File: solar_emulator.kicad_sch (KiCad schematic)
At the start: 57 parts, among them J1 USB_C_Receptacle, J2 Conn_01x02, J3 Conn_01x03, J4 Conn_01x02, J5 Conn_01x02, J6 Conn_01x04, J7 Conn_01x02, Q1 NMOS, Q2 NMOS, Q3 NMOS, Q4 NMOS, Q5 NMOS, Q6 NMOS, Q7 NMOS, Q8 NMOS, SW1 SW_Push, SW2 SW_Push, U1 ESP32-S3-WROOM-1, U2 LD1117S33TR_SOT223, U3 HIP4081AIPZ, U4 HIP4081AIPZ

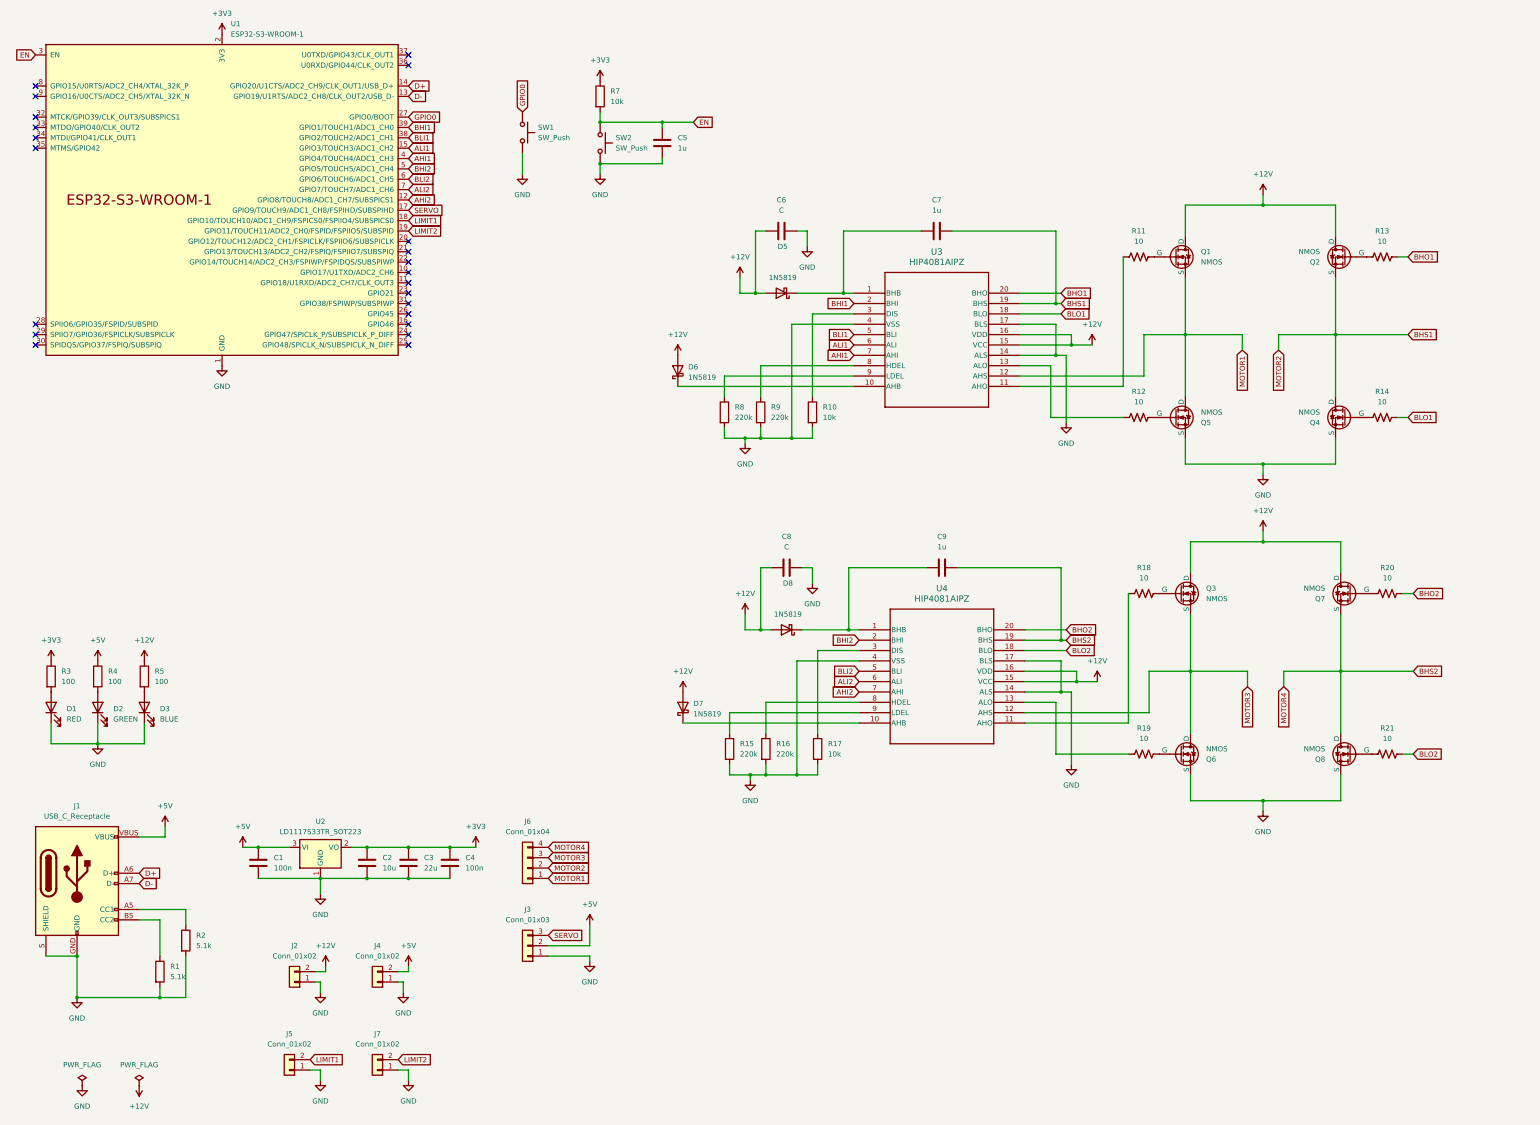
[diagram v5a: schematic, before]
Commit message: assign footprints, import footprints to pcb
start placing components on pcb, seek for advice
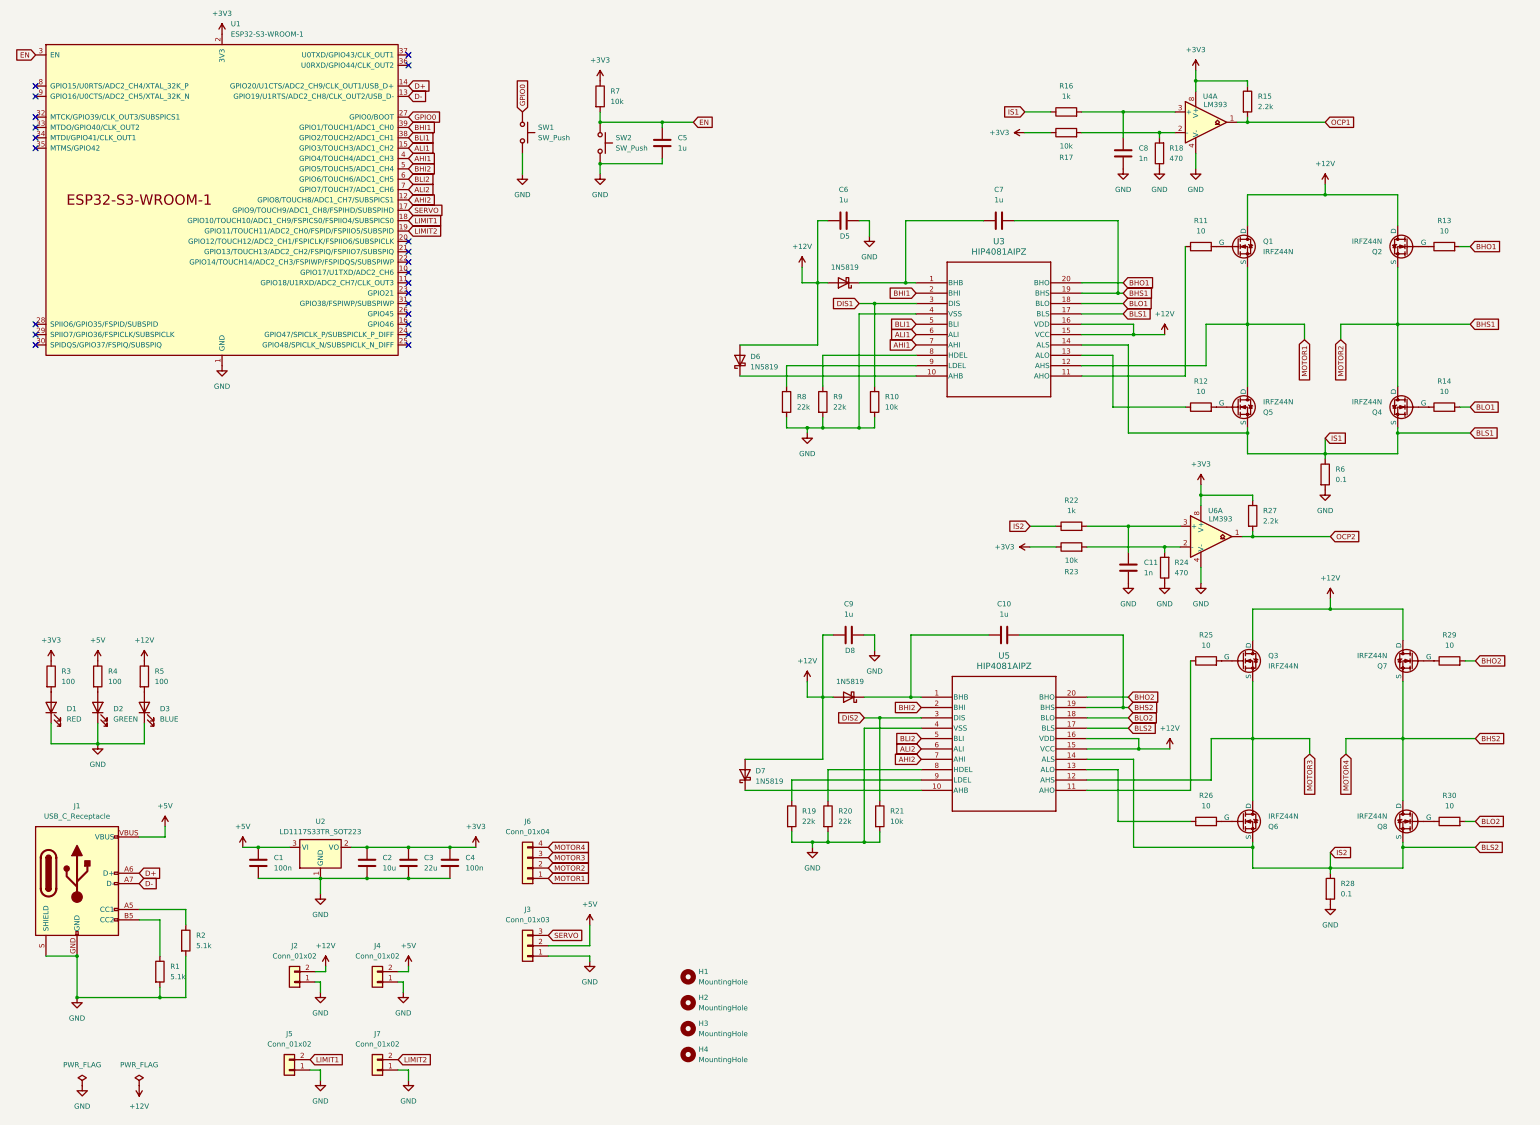
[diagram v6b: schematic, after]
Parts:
- removed R11, R12, R13, R14, R18, R19, R20, R21: 10, SparkFun-Resistor:R_0603_1608Metric, symbol SparkFun-Resistor:R
- removed U4: HIP4081AIPZ, PDIP20_7P11X26P9_INR, symbol custom_lib:HIP4081AIPZ
- added C10: 1u, Capacitor_THT:C_Disc_D4.7mm_W2.5mm_P5.00mm, symbol Device:C
- added C11: 1n, Capacitor_THT:C_Disc_D4.7mm_W2.5mm_P5.00mm, symbol Device:C
- added H1, H2, H3, H4: MountingHole, MountingHole:MountingHole_3.2mm_M3_ISO7380_Pad, symbol Mechanical:MountingHole
- added R11, R12, R13, R14, R25, R26, R29, R30: 10, Resistor_THT:R_Axial_DIN0207_L6.3mm_D2.5mm_P10.16mm_Horizontal, symbol Device:R
- added R18, R24: 470, Resistor_THT:R_Axial_DIN0207_L6.3mm_D2.5mm_P10.16mm_Horizontal, symbol Device:R
- added R19, R20: 22k, Resistor_THT:R_Axial_DIN0207_L6.3mm_D2.5mm_P10.16mm_Horizontal, symbol Device:R
- added R21, R23: 10k, Resistor_THT:R_Axial_DIN0207_L6.3mm_D2.5mm_P10.16mm_Horizontal, symbol Device:R
- added R22: 1k, Resistor_THT:R_Axial_DIN0207_L6.3mm_D2.5mm_P10.16mm_Horizontal, symbol Device:R
- added R27: 2.2k, Resistor_THT:R_Axial_DIN0207_L6.3mm_D2.5mm_P10.16mm_Horizontal, symbol Device:R
- added R28, R6: 0.1, Resistor_THT:R_Axial_DIN0207_L6.3mm_D2.5mm_P15.24mm_Horizontal, symbol Device:R
- added U4, U6: LM393, Package_DIP:DIP-8_W7.62mm, symbol Comparator:LM393
- added U5: HIP4081AIPZ, ul_HIP4081AIPZ:PDIP20_7P11X26P9_INR, symbol custom_lib:HIP4081AIPZ
- C1, C4: footprint (none) -> Capacitor_THT:C_Disc_D9.0mm_W2.5mm_P5.00mm
- C2, C3: footprint (none) -> Capacitor_THT:CP_Radial_D5.0mm_P2.00mm
- C5, C7, C9: footprint (none) -> Capacitor_THT:C_Disc_D4.7mm_W2.5mm_P5.00mm
- C6: value C -> 1u; footprint (none) -> Capacitor_THT:C_Disc_D4.7mm_W2.5mm_P5.00mm
- C8: value C -> 1n; footprint (none) -> Capacitor_THT:C_Disc_D4.7mm_W2.5mm_P5.00mm
- D1, D2, D3: footprint (none) -> LED_THT:LED_D3.0mm
- J2, J4, J5, J7: footprint (none) -> Connector_PinHeader_2.54mm:PinHeader_1x02_P2.54mm_Vertical
- J3: footprint (none) -> Connector_PinHeader_2.54mm:PinHeader_1x03_P2.54mm_Vertical
- J6: footprint (none) -> Connector_PinHeader_2.54mm:PinHeader_1x04_P2.54mm_Vertical
- Q1, Q2, Q3, Q4, Q5, Q6, Q7, Q8: value NMOS -> IRFZ44N; footprint (none) -> Package_TO_SOT_THT:TO-220-3_Vertical
- R1, R10, R17, R2, R3, R4, R5, R7: footprint (none) -> Resistor_THT:R_Axial_DIN0207_L6.3mm_D2.5mm_P10.16mm_Horizontal
- R15: value 220k -> 2.2k; footprint (none) -> Resistor_THT:R_Axial_DIN0207_L6.3mm_D2.5mm_P10.16mm_Horizontal
- R16: value 220k -> 1k; footprint (none) -> Resistor_THT:R_Axial_DIN0207_L6.3mm_D2.5mm_P10.16mm_Horizontal
- R8, R9: value 220k -> 22k; footprint (none) -> Resistor_THT:R_Axial_DIN0207_L6.3mm_D2.5mm_P10.16mm_Horizontal
- SW1, SW2: footprint (none) -> Button_Switch_THT:SW_PUSH_6mm_H4.3mm
- U3: footprint PDIP20_7P11X26P9_INR -> ul_HIP4081AIPZ:PDIP20_7P11X26P9_INR
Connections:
- net +12V: now also C9.1, U5.15 (VCC), U5.16 (VDD); no longer C8.1
- net +3V3: now also R15.1, R17.1, R23.1, R27.1, U4.8 (V+), U6.8 (V+)
- net AHI2: now also U5.7 (AHI)
- net ALI2: now also U5.6 (ALI)
- net BHI2: now also U5.2 (BHI)
- net BHO1: now also R13.2
- net BHO2: now also R29.2, U5.20 (BHO)
- net BHS2: now also C10.2, U5.19 (BHS); no longer C9.2
- net BLI2: now also U5.5 (BLI)
- net BLO1: now also R14.2
- net BLO2: now also R30.2, U5.18 (BLO)
- net GND: now also C9.2, C11.2, R18.1, R19.2, R20.2, R21.2, R24.1, R28.2, R6.2, U4.4 (V-), U5.4 (VSS), U6.4 (V-); no longer Q4.3 (S), Q5.3 (S), Q6.3 (S), Q8.3 (S), R15.2, R16.2, R17.2, U3.14 (ALS), U3.17 (BLS)
- net MOTOR3: now also U5.12 (AHS)
- net at Q1.2 (G): now also R11.2
- net at Q7.2 (G): now also R29.1
- net at U3.11 (AHO): now also R11.1
- net at U3.13 (ALO): now also R12.1
- net DIS1: now reaches R10.1, U3.3 (DIS)
- net at D8.1 (K): now also C10.1, U5.1 (BHB); no longer C9.1
- net at D7.1 (K): now also U5.10 (AHB)
- net BLS1: now reaches R16.1
- net BLS1: now also Q4.3 (S), Q5.3 (S), U3.14 (ALS), U3.17 (BLS), R6.1
- net at Q5.2 (G): now also R12.2
- net at Q4.2 (G): now also R14.1
- net at Q6.2 (G): now also R26.2
- net at Q8.2 (G): now also R30.1
- net at Q2.2 (G): now also R13.1
- net at Q3.2 (G): now also R25.2
- new net: R23.2, R24.2, U6.2 (-)
- new net: C11.1, R22.2, U6.3 (+)
- new net: R25.1, U5.11 (AHO)
- new net: R26.1, U5.13 (ALO)
- new net: R20.1, U5.8 (HDEL)
- new net: R19.1, U5.9 (LDEL)
- new net: R17.2, R18.2, U4.2 (-)
- new net: C8.1, R16.2, U4.3 (+)
- new net BLS2: Q6.3 (S), Q8.3 (S), R22.1, R28.1, U5.14 (ALS), U5.17 (BLS)
- new net DIS2: R21.1, U5.3 (DIS)
- new net OCP1: R15.2, U4.1
- new net OCP2: R27.2, U6.1

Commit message: implement footprints, begin placement of components
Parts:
- C2, C3: footprint Capacitor_THT:CP_Radial_D5.0mm_P2.00mm -> Capacitor_THT:C_Disc_D6.0mm_W2.5mm_P5.00mm
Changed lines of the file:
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@@
 			)
 		)
-		(property "Footprint" "Capacitor_THT:CP_Radial_D5.0mm_P2.00mm"
+		(property "Footprint" "Capacitor_THT:C_Disc_D6.0mm_W2.5mm_P5.00mm"
 			(at 105.1052 226.06 0)
 			(hide yes)
@@
 			)
 		)
-		(property "Footprint" "Capacitor_THT:CP_Radial_D5.0mm_P2.00mm"
+		(property "Footprint" "Capacitor_THT:C_Disc_D6.0mm_W2.5mm_P5.00mm"
 			(at 115.2652 226.06 0)
 			(hide yes)

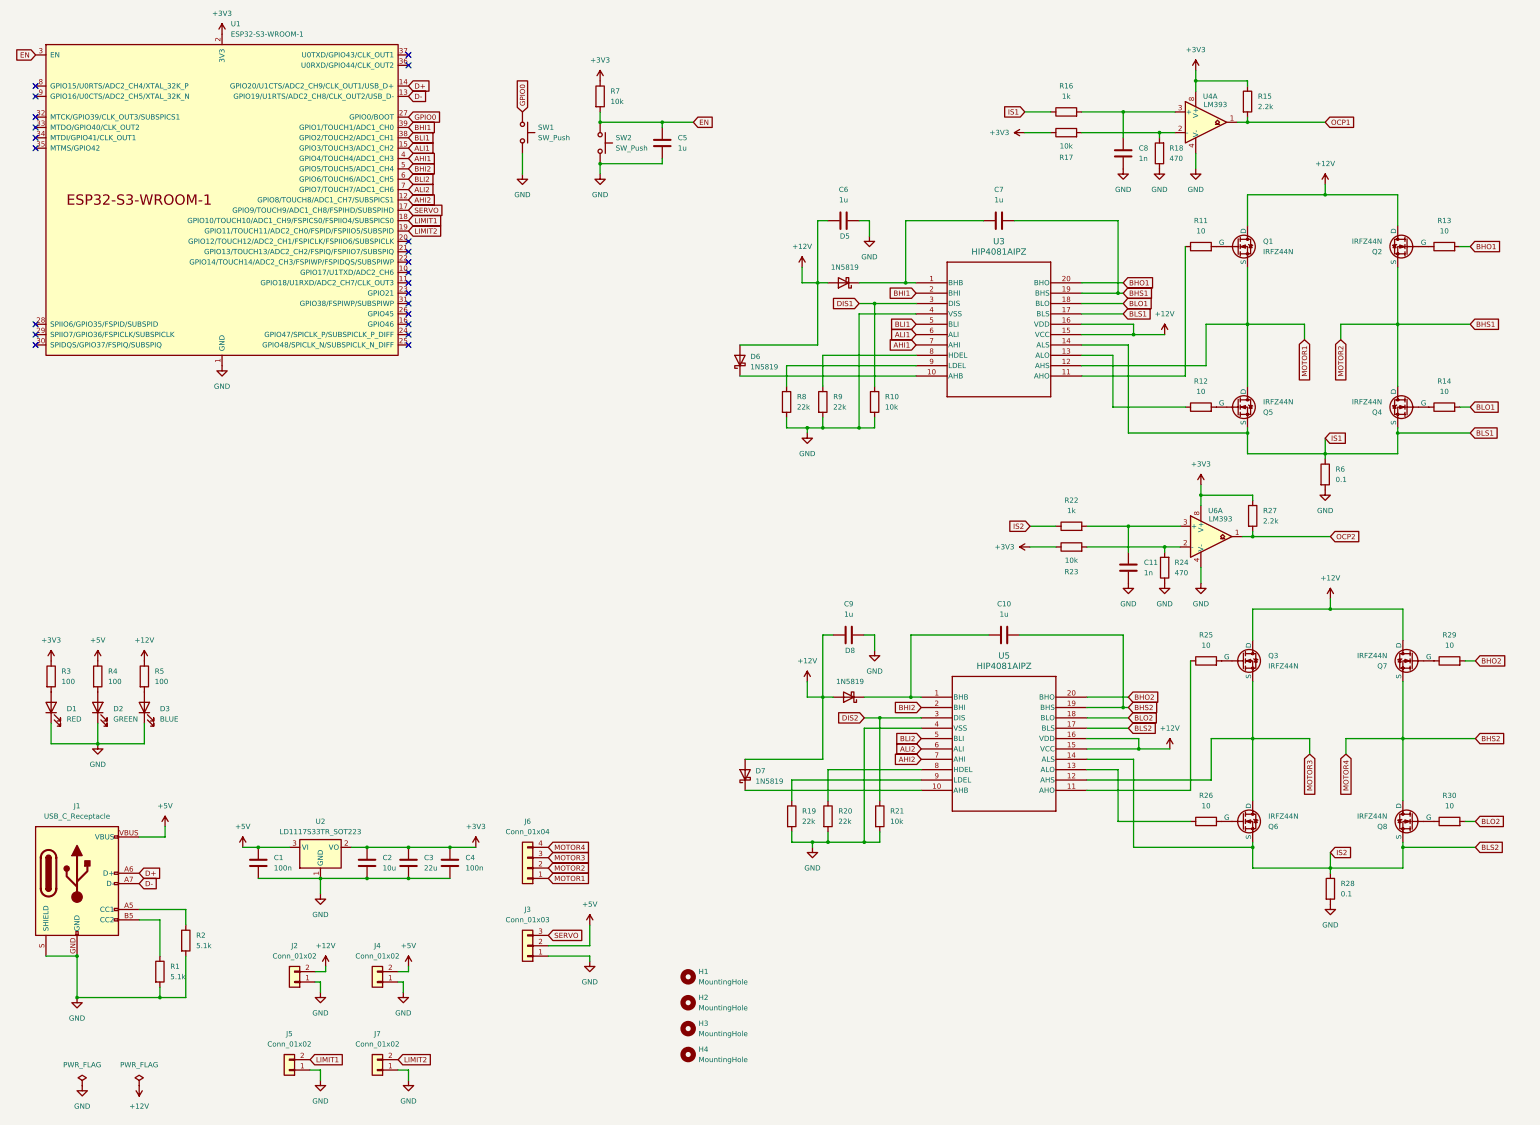
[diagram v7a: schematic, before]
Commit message: component layout complete, ground plane implemented
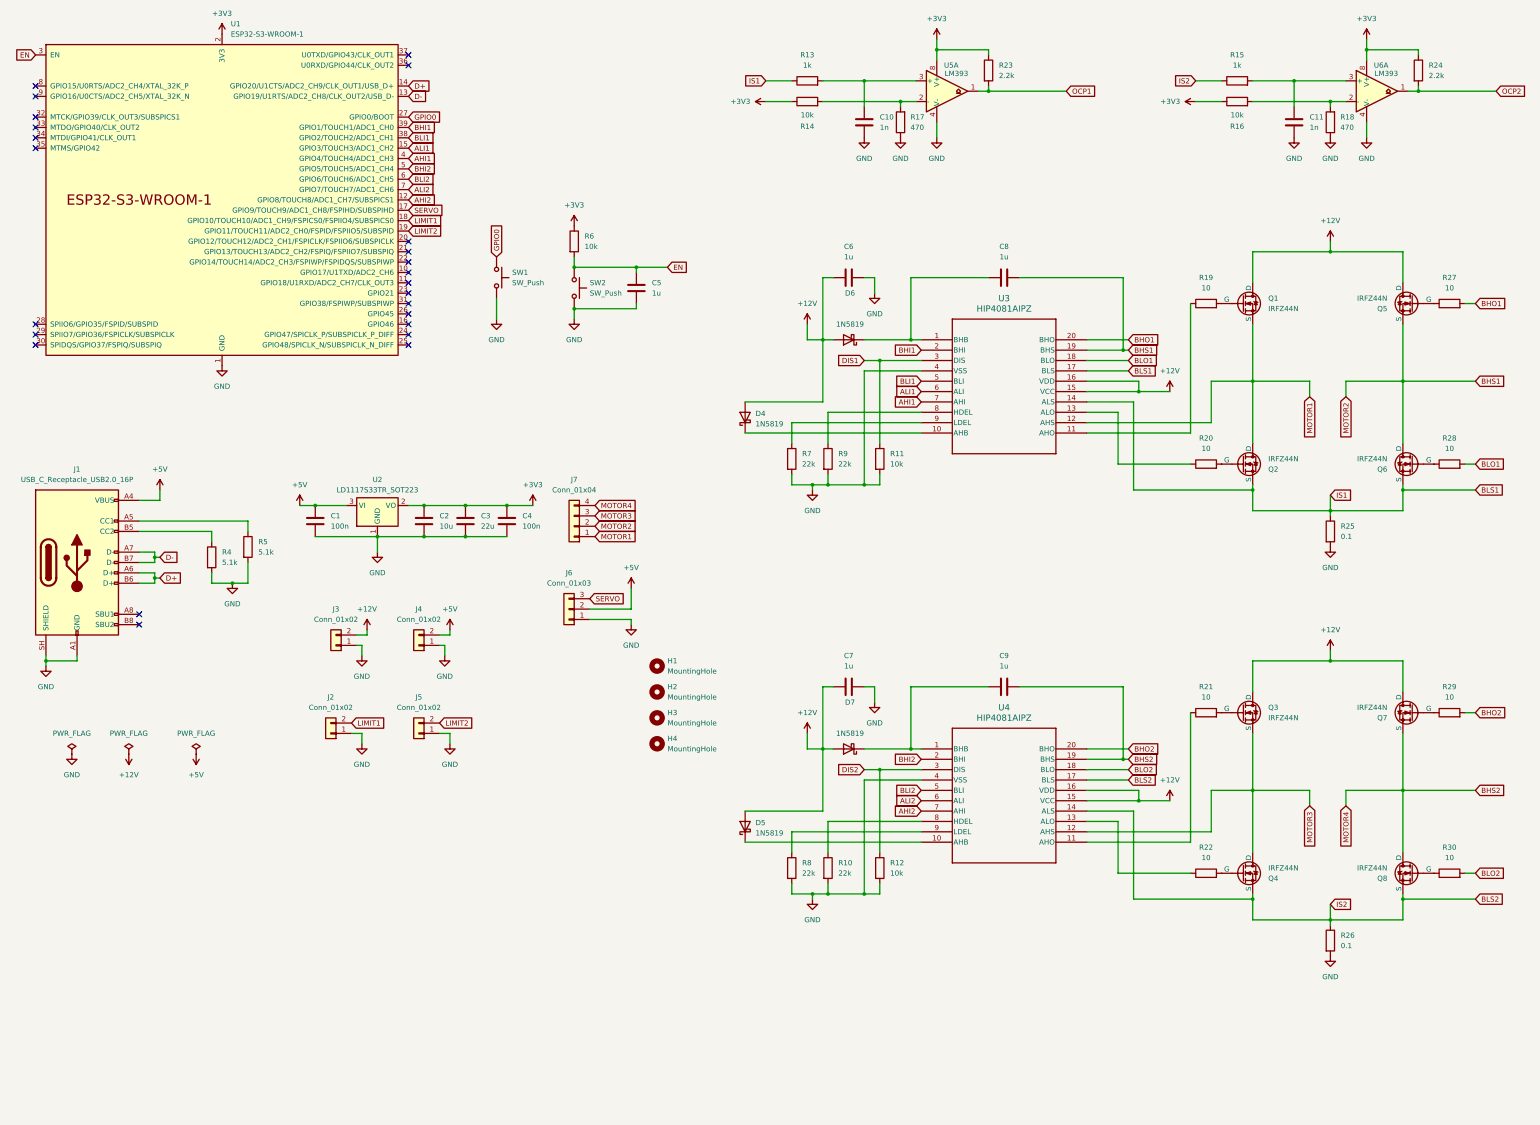
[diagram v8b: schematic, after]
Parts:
- removed D1: RED, LED_THT:LED_D3.0mm, symbol Device:LED
- removed D2: GREEN, LED_THT:LED_D3.0mm, symbol Device:LED
- removed D3: BLUE, LED_THT:LED_D3.0mm, symbol Device:LED
- removed J1: USB_C_Receptacle, SparkFun-Connector:USB-C_16, symbol SparkFun-Connector:USB_C_Receptacle
- removed R1, R2: 5.1k, Resistor_THT:R_Axial_DIN0207_L6.3mm_D2.5mm_P10.16mm_Horizontal, symbol Device:R
- removed R3: 100, Resistor_THT:R_Axial_DIN0207_L6.3mm_D2.5mm_P10.16mm_Horizontal, symbol Device:R
- added J1: USB_C_Receptacle_USB2.0_16P, Connector_USB:USB_C_Receptacle_HRO_TYPE-C-31-M-12, symbol Connector:USB_C_Receptacle_USB2.0_16P
- R4, R5: value 100 -> 5.1k
- renumbered C8 to C10, C9 to C7, C7 to C8, C10 to C9, D6 to D4, D7 to D5, D5 to D6, D8 to D7, J5 to J2, J2 to J3, J7 to J5, J3 to J6, J6 to J7, Q5 to Q2, Q6 to Q4, Q2 to Q5, Q4 to Q6, R20 to R10, R10 to R11, R21 to R12, R16 to R13, R17 to R14, R22 to R15, R23 to R16, R18 to R17, R24 to R18, R11 to R19, R12 to R20, R25 to R21, R26 to R22, R15 to R23, R27 to R24, R6 to R25, R28 to R26, R13 to R27, R14 to R28, R7 to R6, R8 to R7, R19 to R8, U5 to U4, U4 to U5
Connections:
- net +12V: no longer R5.1
- net +5V: now also J1.A4 (VBUS), J1.A9 (VBUS), J1.B4 (VBUS), J1.B9 (VBUS); no longer R4.1
- net D+: now also J1.A6 (D+), J1.B6 (D+)
- net D-: now also J1.A7 (D-), J1.B7 (D-)
- net GND: now also R4.2, R5.2, J1.A1 (GND), J1.A12 (GND), J1.B1 (GND), J1.B12 (GND), J1.SH (SHIELD)
- new net: J1.A5 (CC1), R5.1
- new net: J1.B5 (CC2), R4.1
- no-connect marks 22 -> 24
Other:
- moved on the sheet: C1, C10, C11, C2, C3, C4, C5, C6, C7, C8, C9, D4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
